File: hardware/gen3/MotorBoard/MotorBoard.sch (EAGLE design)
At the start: 245 parts, among them M10O1 TEST_PT, M1O2 TEST_PT, M1O3 TEST_PT, M2O1 TEST_PT, M2O2 TEST_PT, M2O3 TEST_PT, M3O1 TEST_PT, M3O2 TEST_PT, M3O3 TEST_PT, M4O1 TEST_PT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

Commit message: fixed weird package issues
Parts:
- C17, C35: device SparkFun-Passives:CAP1206 -> SparkFun-Passives:CAP0805
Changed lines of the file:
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@@
 <part name="R104" library="SparkFun-Resistors" deviceset="RESISTOR" device="0805-RES" value="37.5k"/>
 <part name="C8" library="SparkFun-Passives" deviceset="CAP" device="0805" value=".1uF"/>
-<part name="C17" library="SparkFun-Passives" deviceset="CAP" device="1206" value=".1uF"/>
+<part name="C17" library="SparkFun-Passives" deviceset="CAP" device="0805" value=".1uF"/>
 <part name="C26" library="SparkFun-Passives" deviceset="CAP" device="0805" value=".1uF"/>
-<part name="C35" library="SparkFun-Passives" deviceset="CAP" device="1206" value=".1uF"/>
+<part name="C35" library="SparkFun-Passives" deviceset="CAP" device="0805" value=".1uF"/>
 <part name="C44" library="SparkFun-Passives" deviceset="CAP" device="0805" value=".1uF"/>
 <part name="C45" library="SparkFun-Passives" deviceset="CAP" device="0805" value=".1uF"/>

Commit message: schematic for differential amp
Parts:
- removed R90: 4.75k, SparkFun-Resistors:RESISTOR0805-RES
- removed RFILT: 15k, SparkFun-Resistors:RESISTOR0805-RES
- added R74, R75: 5k, SparkFun-Passives:RESISTOR0805-RES
- added R76: 75k, SparkFun-Passives:RESISTOR0805-RES
- C1: value .1uF -> .3uF
- R89: value 66.5k -> 75k; device SparkFun-Resistors:RESISTOR0805-RES -> SparkFun-Passives:RESISTOR0805-RES
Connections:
- removed net N$109: OP1.-IN, R89.1, R90.2
- new net N$92: C1.1, OP1.-IN, R75.2, R89.1
- net 12VGND: now also R75.1
- net GND: now also R76.2; no longer C1.2, R90.1
- net N$46: now also C1.2, R74.2, R76.1; no longer C1.1, RFILT.2
- net O1: now also R74.1; no longer RFILT.1
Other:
- note added: "lowpass, f3db = 106 hz"
- moved on the sheet: C1, LSS1, OP1, R89, R93, R94, RSENSE1, SENSE1

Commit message: diff amp for all motors. added comments to schematics
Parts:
- removed RFILT1, RFILT3, RFILT4: 15k, SparkFun-Resistors:RESISTOR0805-RES
- added R108, R111, R112: 75k, SparkFun-Passives:RESISTOR0805-RES
- added R109, R110, R90: 5k, SparkFun-Passives:RESISTOR0805-RES
- C2, C41, C42: value .1uF -> .3uF
- R100, R86: value 4.75k -> 75k; device SparkFun-Resistors:RESISTOR0805-RES -> SparkFun-Passives:RESISTOR0805-RES
- R60, R98: value 66.5k -> 5k; device SparkFun-Resistors:RESISTOR0805-RES -> SparkFun-Passives:RESISTOR0805-RES
- R61: value 4.75k -> 5k; device SparkFun-Resistors:RESISTOR0805-RES -> SparkFun-Passives:RESISTOR0805-RES
- R83: value 66.5k -> 75k; device SparkFun-Resistors:RESISTOR0805-RES -> SparkFun-Passives:RESISTOR0805-RES
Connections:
- net 12VGND: now also R110.1, R61.1, R98.1
- net GND: now also R100.2, R111.2, R83.2; no longer C2.2, C41.2, C42.2, R100.1, R61.1, R86.1
- net N$15: now also OP2.-IN, R61.2, R86.1; no longer OP2.+IN, RFILT1.2
- net N$2: now also C2.2, OP2.+IN, R60.2, R83.1; no longer OP2.-IN, R60.1, R61.2
- net N$67: now also C41.2, OP3.+IN, R100.1, R90.2; no longer OP4.-IN, R83.1, R86.2
- net N$87: now also OP3.-IN, R108.1, R98.2; no longer OP4.+IN, RFILT4.2
- net N$89: now also C42.2, OP4.+IN, R109.2, R111.1; no longer OP3.-IN, R100.2, R98.1
- net N$90: now also OP4.-IN, R110.2, R112.1; no longer OP3.+IN, RFILT3.2
- net O2: now also R60.1; no longer RFILT1.1
- net O3: now also R109.1; no longer RFILT3.1
- net O4: now also R90.1; no longer RFILT4.1
- net SENSE2: now also R86.2; no longer R60.2
- net SENSE3: now also OP4.OUT, R112.2; no longer OP3.OUT, R98.2
- net SENSE4: now also OP3.OUT, R108.2; no longer OP4.OUT, R83.2
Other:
- note added: "Allegro A4915 Motor Driver. Takes in a PWM and outputs 6 gate drives. careful, 180 degrees"
- note added: "Differential amplifier to measure current through the motor. Low pass to average current throughout PWM cycle."
- note added: "Overcurrent shutoff comparator. Will block PWM signal when current is higher than 6A. (limit set by reference voltage)"
- note added: "watch out for the weird hall order from the motor..."
- note removed: "careful, 180 degrees"
- note removed: "lowpass, f3db = 120 hz"
- moved on the sheet: C2, C41, C42, LSS2, LSS3, LSS4, OP2, OP3, OP4, R100, R60, R61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

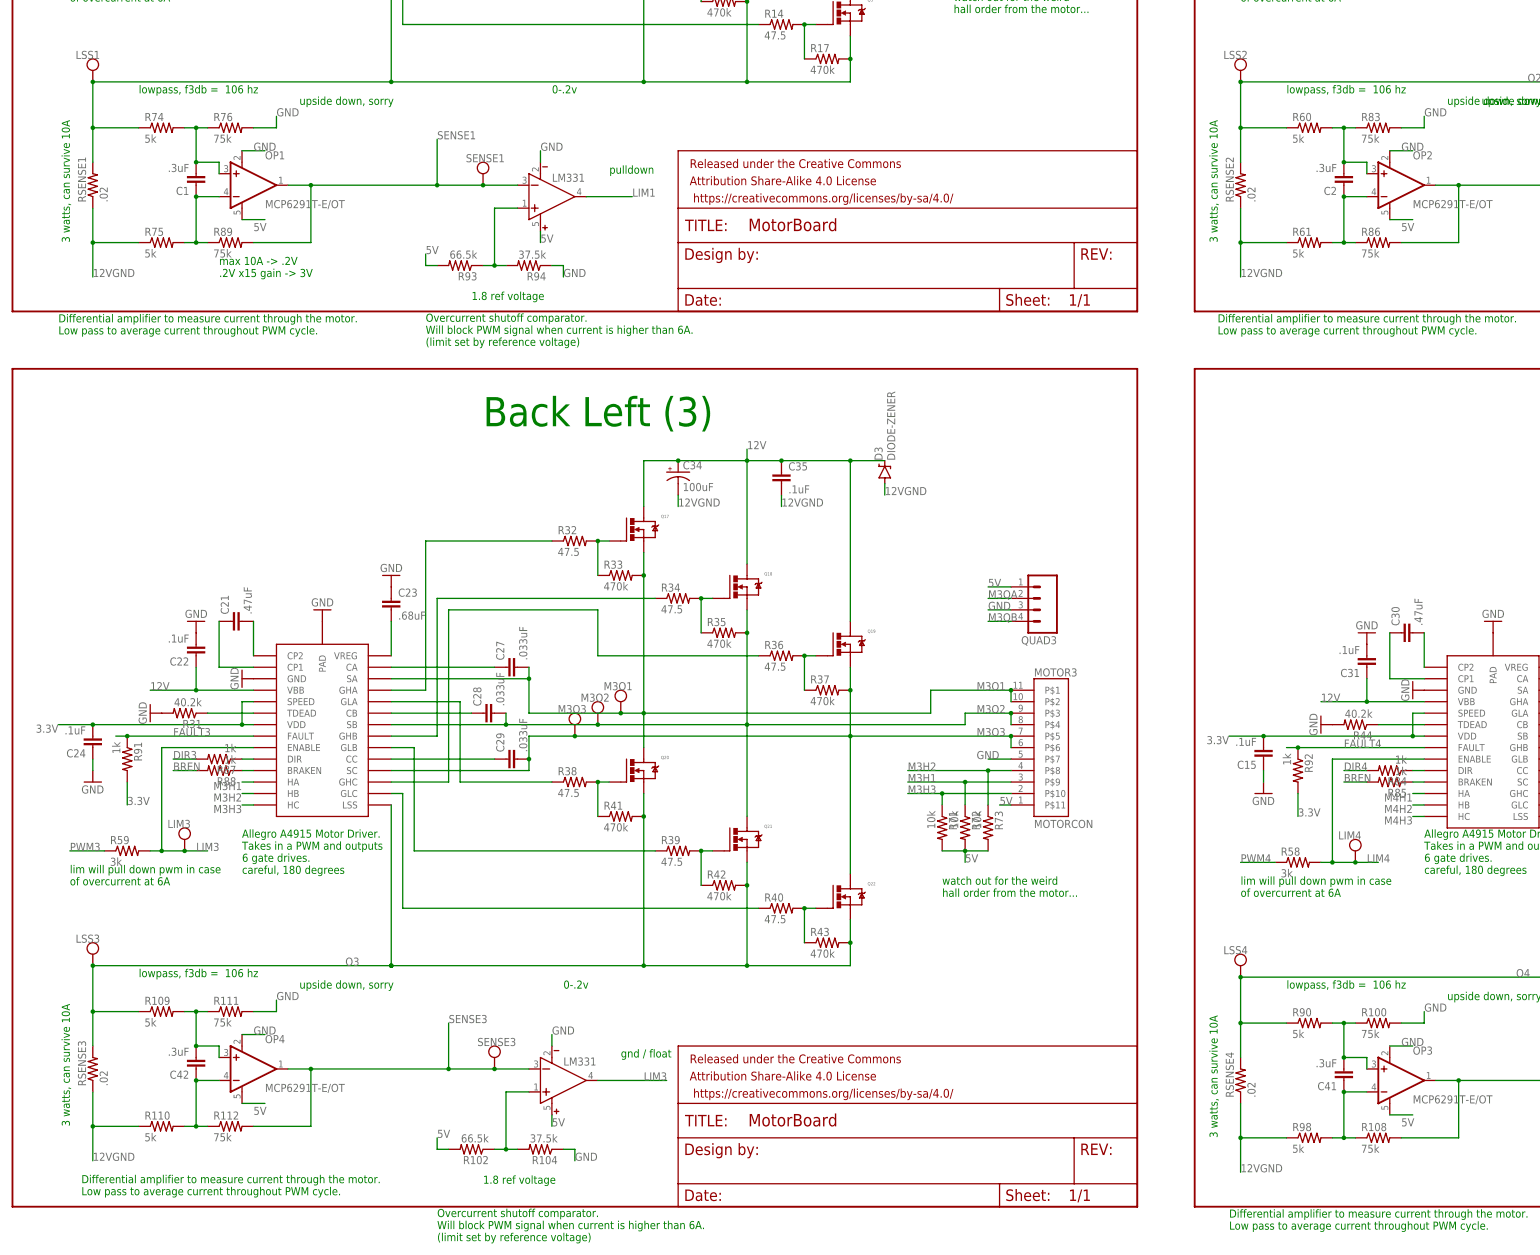
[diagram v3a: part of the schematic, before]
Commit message: fixed diff amp. again
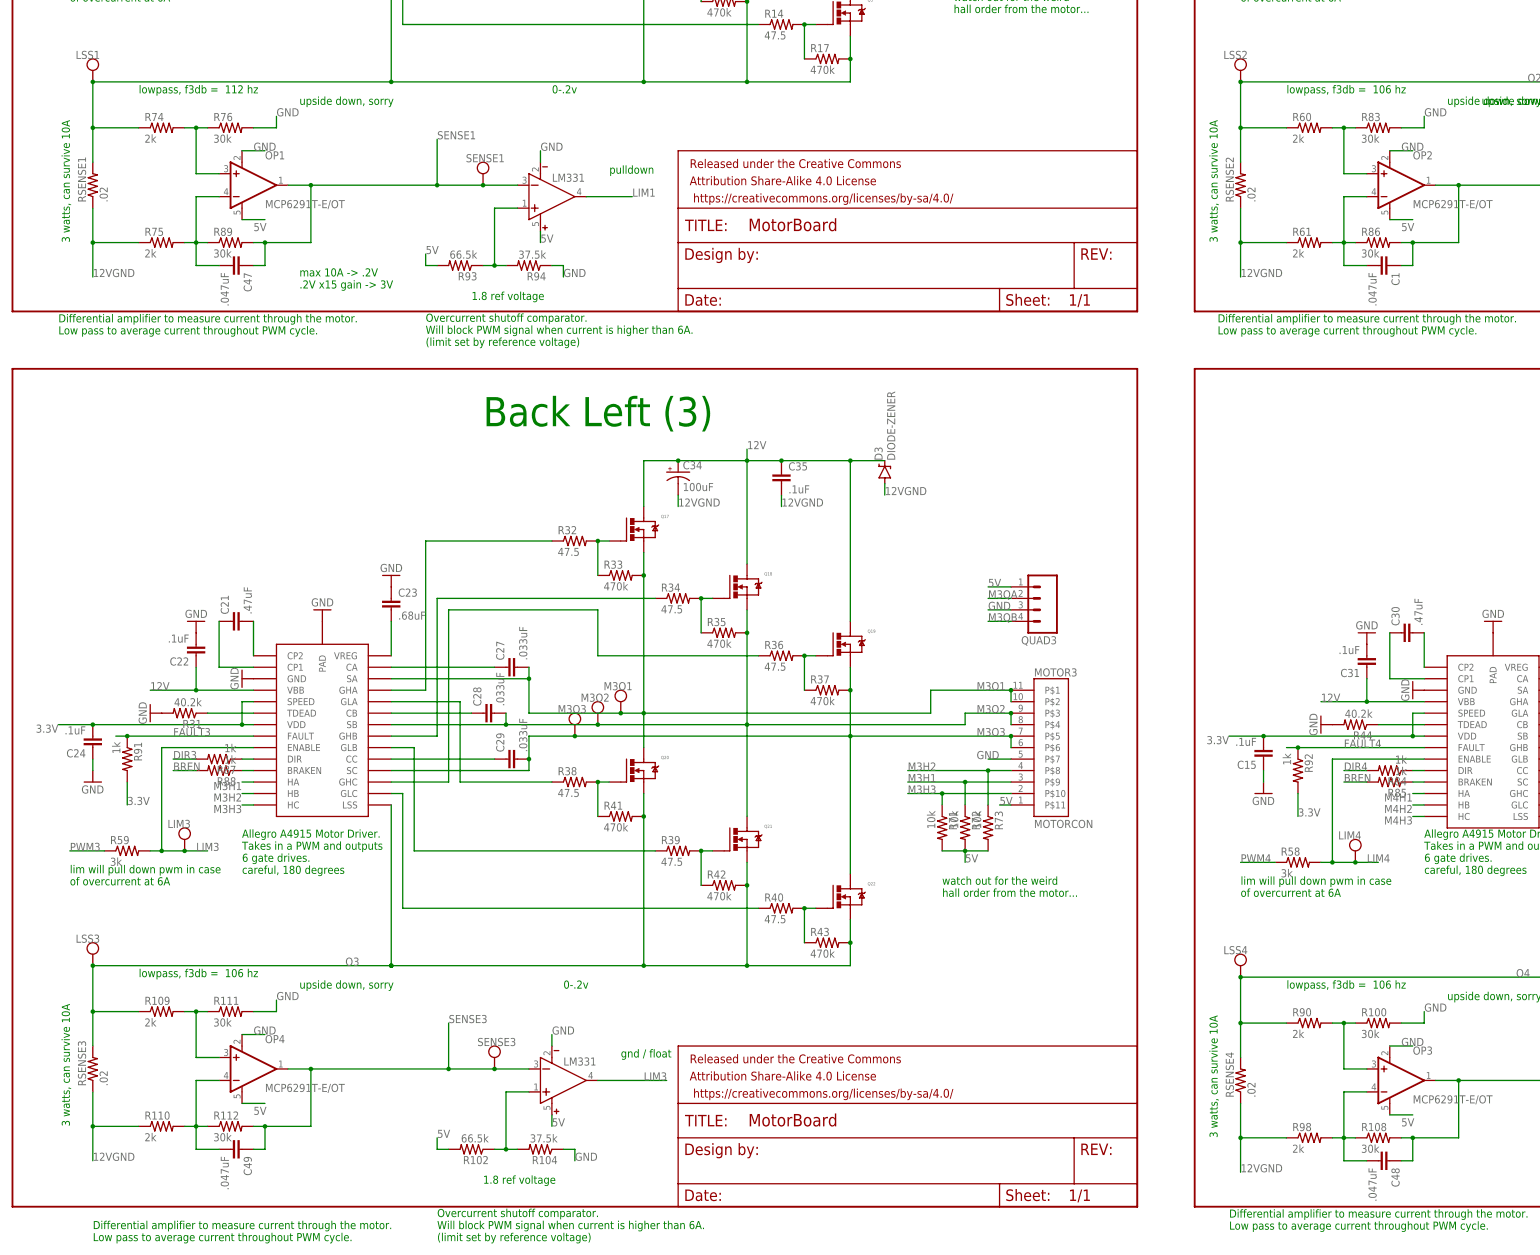
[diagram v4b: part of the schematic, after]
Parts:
- removed C2, C41, C42: .3uF, SparkFun-Passives:CAP0805
- added C47, C48, C49: .047uF, SparkFun-Passives:CAP0805
- C1: value .3uF -> .047uF
- R100, R108, R111, R112, R76, R83, R86, R89: value 75k -> 30k
- R109, R110, R60, R61, R74, R75, R90, R98: value 5k -> 2k
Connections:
- net N$15: now also C1.2; no longer C2.1
- net N$2: no longer C2.2
- net N$46: no longer C1.2
- net N$67: no longer C41.2
- net N$87: now also C48.2; no longer C41.1
- net N$89: no longer C42.2
- net N$90: now also C49.2; no longer C42.1
- net N$92: now also C47.2; no longer C1.1
- net SENSE1: now also C47.1
- net SENSE2: now also C1.1
- net SENSE3: now also C49.1
- net SENSE4: now also C48.1
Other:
- note added: "lowpass, f3db = 112 hz"
- moved on the sheet: C1

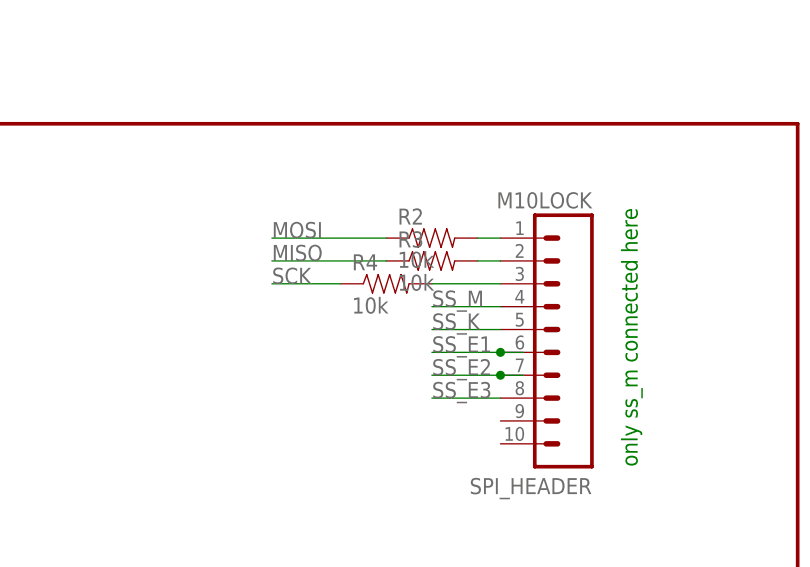
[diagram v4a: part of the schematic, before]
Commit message: some decoupling for power lines
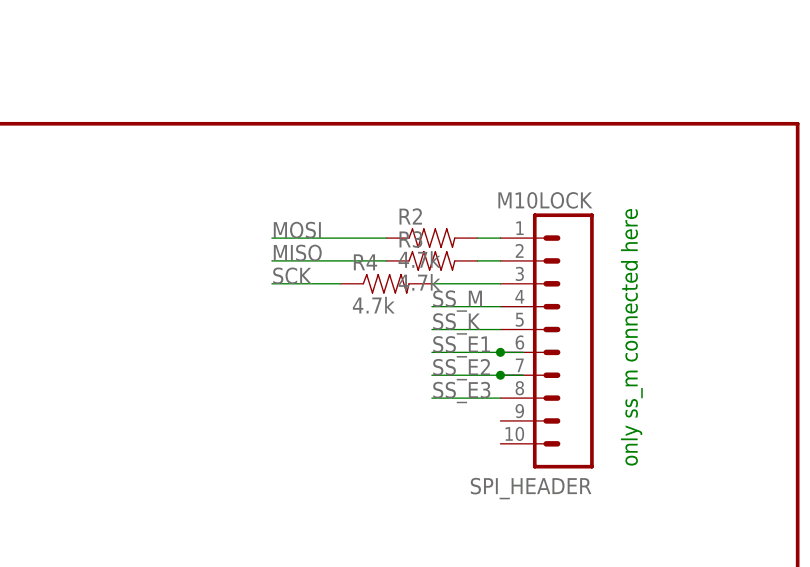
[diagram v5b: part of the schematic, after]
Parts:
- R2, R3, R4: value 10k -> 4.7k
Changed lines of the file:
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@@
 <part name="POWER_HEADER" library="SparkFun-Connectors" deviceset="M10" device="LOCK" value="M10LOCK"/>
 <part name="SPARE_HEADER" library="SparkFun-Connectors" deviceset="M10" device="LOCK" value="M10LOCK"/>
-<part name="R2" library="SparkFun-Passives" deviceset="RESISTOR" device="0805-RES" value="10k"/>
-<part name="R3" library="SparkFun-Passives" deviceset="RESISTOR" device="0805-RES" value="10k"/>
-<part name="R4" library="SparkFun-Passives" deviceset="RESISTOR" device="0805-RES" value="10k"/>
+<part name="R2" library="SparkFun-Passives" deviceset="RESISTOR" device="0805-RES" value="4.7k"/>
+<part name="R3" library="SparkFun-Passives" deviceset="RESISTOR" device="0805-RES" value="4.7k"/>
+<part name="R4" library="SparkFun-Passives" deviceset="RESISTOR" device="0805-RES" value="4.7k"/>
 <part name="U$4" library="rfc" deviceset="A4915" device=""/>
 <part name="C3" library="SparkFun-Passives" deviceset="CAP" device="0805" value=".47uF"/>
